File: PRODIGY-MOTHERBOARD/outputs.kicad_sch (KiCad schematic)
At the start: 20 parts, among them J10 GPIO, J11 SPI_OUT, J12 I2C, J13 CAN, J14 SERIAL, J15 12V OUT, J16 SERVO, J17 SERVO, J18 SERVO, J19 Ultrasonic, J20 MOTOR, J3 A_IN, J4 USB_A, J5 A_OUT, J6 Neopixel, J7 GPIO, J8 GPIO, J9 GPIO

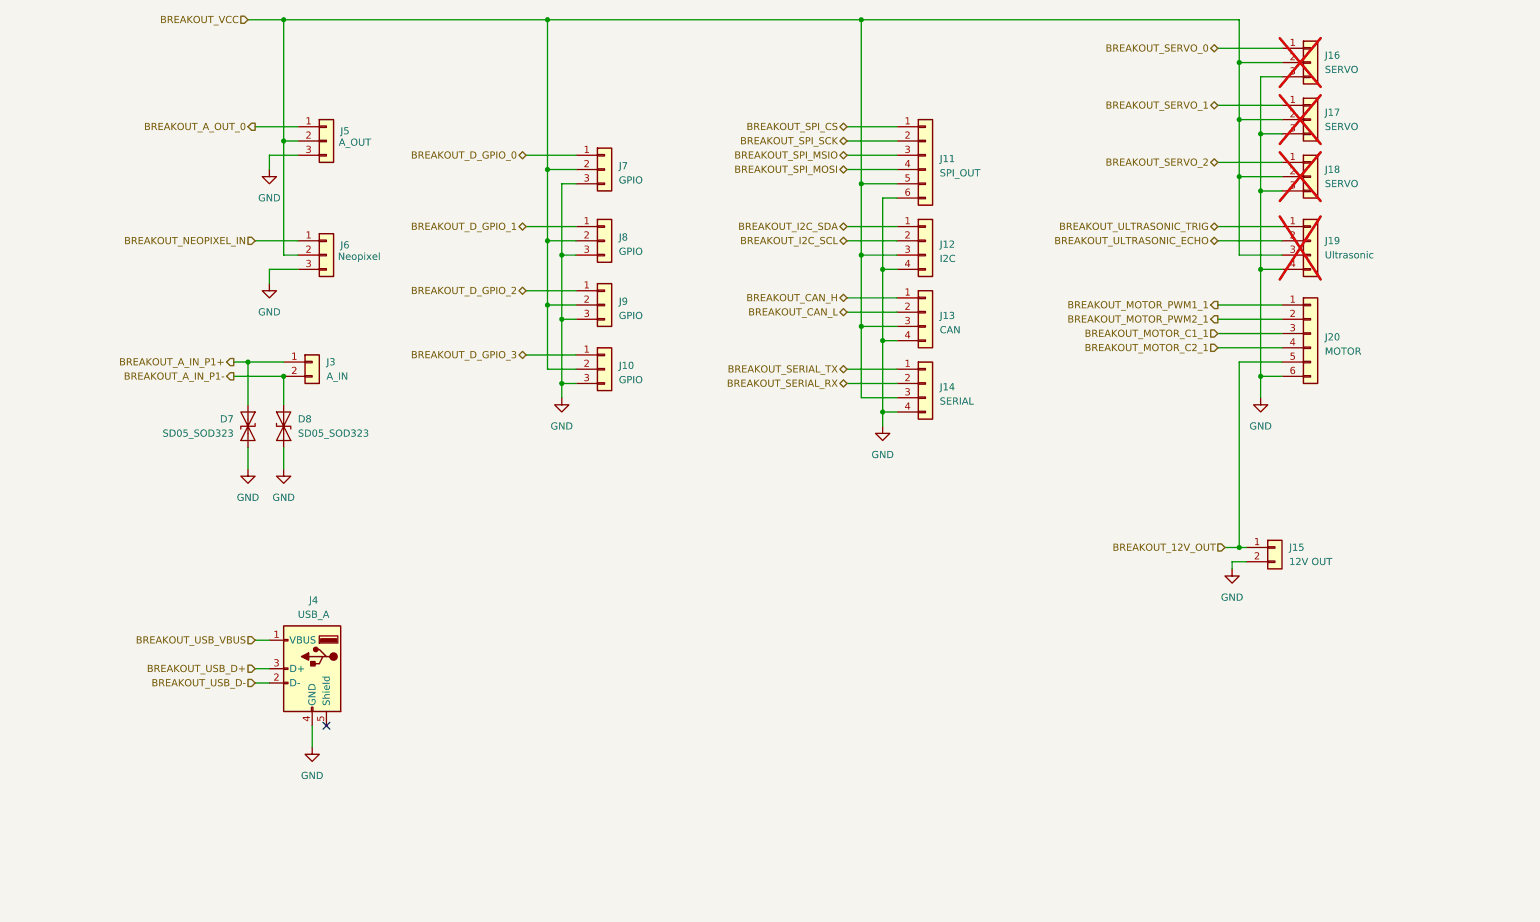
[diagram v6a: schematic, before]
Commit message: Added proper debounce filter elements to buttons.
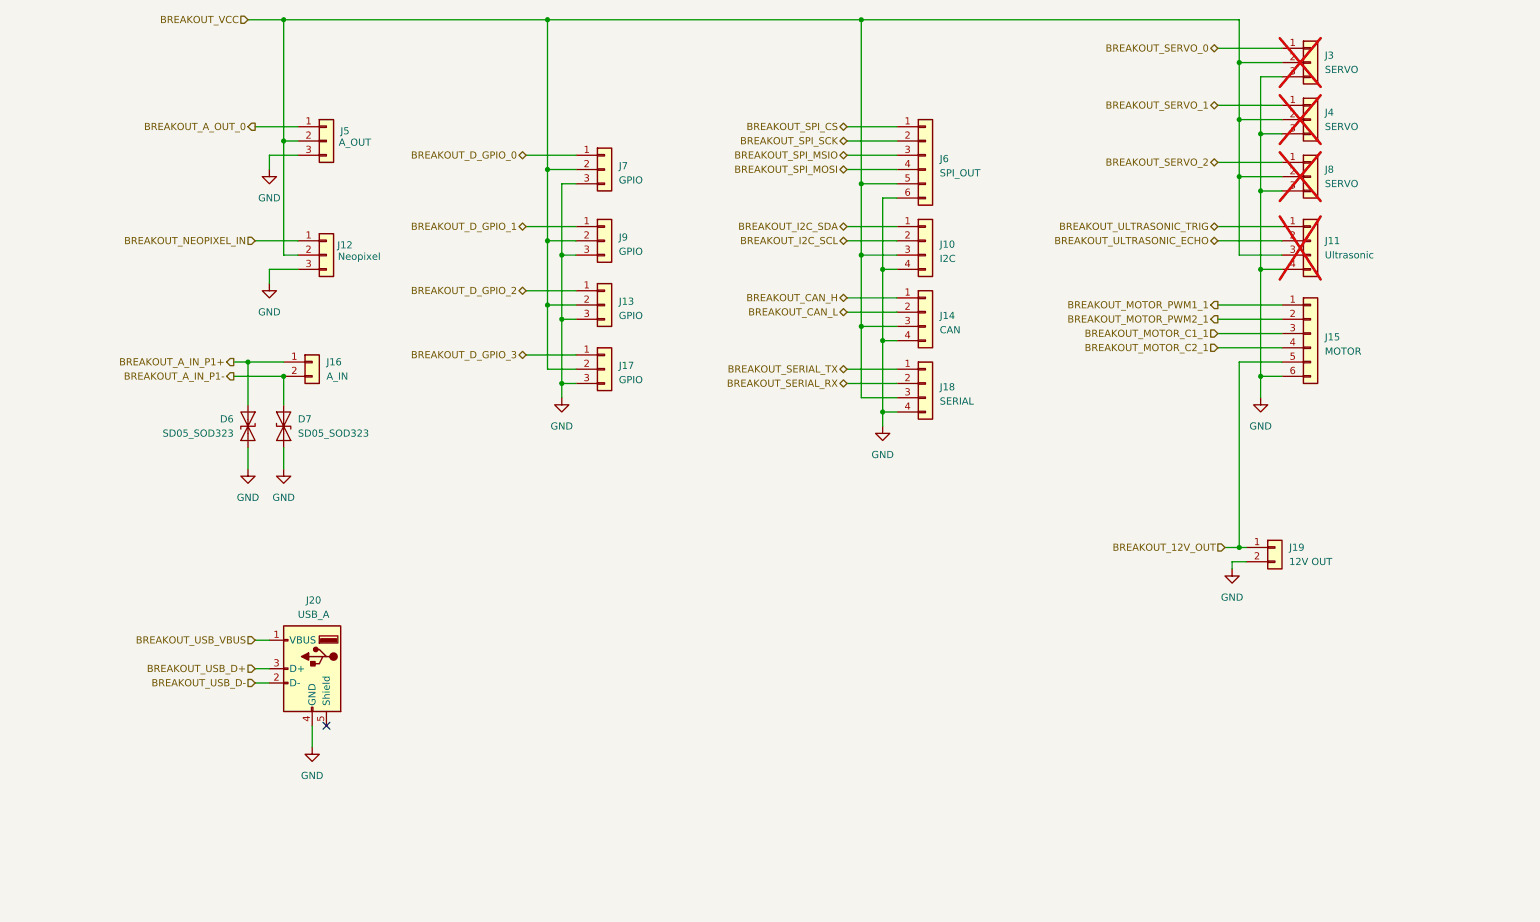
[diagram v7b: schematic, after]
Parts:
- renumbered D7 to D6, D8 to D7, J12 to J10, J19 to J11, J6 to J12, J9 to J13, J13 to J14, J20 to J15, J3 to J16, J10 to J17, J14 to J18, J15 to J19, J4 to J20, J16 to J3, J17 to J4, J11 to J6, J18 to J8, J8 to J9
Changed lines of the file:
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@@
 		(dnp no)
 		(fields_autoplaced yes)
-		(property "Reference" "#PWR013"
+		(property "Reference" "#PWR014"
 			(at 62.23 81.28 0)
 			(effects
@@
 			(project "PRODIGY-MOTHERBOARD"
 				(path "/f1c25860-8989-4190-bd24-2491d23ca7d9/a962dcec-9dee-4e54-acaa-e8da87dab487"
-					(reference "#PWR013")
+					(reference "#PWR014")
 					(unit 1)
 				)
@@
 		(dnp no)
 		(fields_autoplaced yes)
-		(property "Reference" "J20"
+		(property "Reference" "J15"
 			(at 250.19 84.455 0)
 			(effects
@@
 			(project "PRODIGY-MOTHERBOARD"
 				(path "/f1c25860-8989-4190-bd24-2491d23ca7d9/a962dcec-9dee-4e54-acaa-e8da87dab487"
-					(reference "J20")
+					(reference "J15")
 					(unit 1)
 				)
@@
 		(on_board yes)
 		(dnp no)
-		(property "Reference" "J4"
+		(property "Reference" "J20"
 			(at 70.104 131.318 0)
 			(effects
@@
 			(project "PRODIGY-MOTHERBOARD"
 				(path "/f1c25860-8989-4190-bd24-2491d23ca7d9/a962dcec-9dee-4e54-acaa-e8da87dab487"
-					(reference "J4")
+					(reference "J20")
 					(unit 1)
 				)
@@
 		(dnp no)
 		(fields_autoplaced yes)
-		(property "Reference" "#PWR018"
+		(property "Reference" "#PWR016"
 			(at 238.76 101.6 0)
 			(effects
@@
 			(project "PRODIGY-MOTHERBOARD"
 				(path "/f1c25860-8989-4190-bd24-2491d23ca7d9/a962dcec-9dee-4e54-acaa-e8da87dab487"
-					(reference "#PWR018")
+					(reference "#PWR016")
 					(unit 1)
 				)
@@
 		(dnp no)
 		(fields_autoplaced yes)
-		(property "Reference" "D7"
+		(property "Reference" "D6"
 			(at 55.88 99.0599 90)
 			(effects
@@
 			(project "PRODIGY-MOTHERBOARD"
 				(path "/f1c25860-8989-4190-bd24-2491d23ca7d9/a962dcec-9dee-4e54-acaa-e8da87dab487"
-					(reference "D7")
+					(reference "D6")
 					(unit 1)
 				)
@@
 		(dnp no)
 		(fields_autoplaced yes)
-		(property "Reference" "D8"
+		(property "Reference" "D7"
 			(at 67.31 99.0599 90)
 			(effects
@@
 			(project "PRODIGY-MOTHERBOARD"
 				(path "/f1c25860-8989-4190-bd24-2491d23ca7d9/a962dcec-9dee-4e54-acaa-e8da87dab487"
-					(reference "D8")
+					(reference "D7")
 					(unit 1)
 				)
@@
 		(dnp no)
 		(fields_autoplaced yes)
-		(property "Reference" "J9"
+		(property "Reference" "J13"
 			(at 124.46 78.105 0)
 			(effects
@@
 			(project "PRODIGY-MOTHERBOARD"
 				(path "/f1c25860-8989-4190-bd24-2491d23ca7d9/a962dcec-9dee-4e54-acaa-e8da87dab487"
-					(reference "J9")
+					(reference "J13")
 					(unit 1)
 				)
@@
 		(dnp no)
 		(fields_autoplaced yes)
-		(property "Reference" "J12"
+		(property "Reference" "J10"
 			(at 181.61 67.945 0)
 			(effects
@@
 			(project "PRODIGY-MOTHERBOARD"
 				(path "/f1c25860-8989-4190-bd24-2491d23ca7d9/a962dcec-9dee-4e54-acaa-e8da87dab487"
-					(reference "J12")
+					(reference "J10")
 					(unit 1)
 				)
@@
 		(dnp no)
 		(fields_autoplaced yes)
-		(property "Reference" "#PWR014"
+		(property "Reference" "#PWR021"
 			(at 69.85 163.83 0)
 			(effects
@@
 			(project "PRODIGY-MOTHERBOARD"
 				(path "/f1c25860-8989-4190-bd24-2491d23ca7d9/a962dcec-9dee-4e54-acaa-e8da87dab487"
-					(reference "#PWR014")
+					(reference "#PWR021")
 					(unit 1)
 				)
@@
 		(dnp yes)
 		(fields_autoplaced yes)
-		(property "Reference" "J16"
+		(property "Reference" "J3"
 			(at 250.19 34.2899 0)
 			(effects
@@
 			(project "PRODIGY-MOTHERBOARD"
 				(path "/f1c25860-8989-4190-bd24-2491d23ca7d9/a962dcec-9dee-4e54-acaa-e8da87dab487"
-					(reference "J16")
+					(reference "J3")
 					(unit 1)
 				)
@@
 		(dnp no)
 		(fields_autoplaced yes)
-		(property "Reference" "J15"
+		(property "Reference" "J19"
 			(at 243.84 121.9199 0)
 			(effects
@@
 			(project "PRODIGY-MOTHERBOARD"
 				(path "/f1c25860-8989-4190-bd24-2491d23ca7d9/a962dcec-9dee-4e54-acaa-e8da87dab487"
-					(reference "J15")
+					(reference "J19")
 					(unit 1)
 				)
@@
 		(dnp no)
 		(fields_autoplaced yes)
-		(property "Reference" "#PWR0114"
+		(property "Reference" "#PWR019"
 			(at 64.77 114.3 0)
 			(effects
@@
 			(project "PRODIGY-MOTHERBOARD"
 				(path "/f1c25860-8989-4190-bd24-2491d23ca7d9/a962dcec-9dee-4e54-acaa-e8da87dab487"
-					(reference "#PWR0114")
+					(reference "#PWR019")
 					(unit 1)
 				)
@@
 		(dnp no)
 		(fields_autoplaced yes)
-		(property "Reference" "#PWR016"
+		(property "Reference" "#PWR017"
 			(at 171.45 106.68 0)
 			(effects
@@
 			(project "PRODIGY-MOTHERBOARD"
 				(path "/f1c25860-8989-4190-bd24-2491d23ca7d9/a962dcec-9dee-4e54-acaa-e8da87dab487"
-					(reference "#PWR016")
+					(reference "#PWR017")
 					(unit 1)
 				)
@@
 		(dnp no)
 		(fields_autoplaced yes)
-		(property "Reference" "#PWR017"
+		(property "Reference" "#PWR020"
 			(at 233.68 132.08 0)
 			(effects
@@
 			(project "PRODIGY-MOTHERBOARD"
 				(path "/f1c25860-8989-4190-bd24-2491d23ca7d9/a962dcec-9dee-4e54-acaa-e8da87dab487"
-					(reference "#PWR017")
+					(reference "#PWR020")
 					(unit 1)
 				)
@@
 		(dnp yes)
 		(fields_autoplaced yes)
-		(property "Reference" "J17"
+		(property "Reference" "J4"
 			(at 250.19 44.4499 0)
 			(effects
@@
 			(project "PRODIGY-MOTHERBOARD"
 				(path "/f1c25860-8989-4190-bd24-2491d23ca7d9/a962dcec-9dee-4e54-acaa-e8da87dab487"
-					(reference "J17")
+					(reference "J4")
 					(unit 1)
 				)
@@
 		(dnp no)
 		(fields_autoplaced yes)
-		(property "Reference" "J3"
+		(property "Reference" "J16"
 			(at 72.39 88.8999 0)
 			(effects
@@
 			(project "PRODIGY-MOTHERBOARD"
 				(path "/f1c25860-8989-4190-bd24-2491d23ca7d9/a962dcec-9dee-4e54-acaa-e8da87dab487"
-					(reference "J3")
+					(reference "J16")
 					(unit 1)
 				)
@@
 		(dnp no)
 		(fields_autoplaced yes)
-		(property "Reference" "J8"
+		(property "Reference" "J9"
 			(at 124.46 66.675 0)
 			(effects
@@
 			(project "PRODIGY-MOTHERBOARD"
 				(path "/f1c25860-8989-4190-bd24-2491d23ca7d9/a962dcec-9dee-4e54-acaa-e8da87dab487"
-					(reference "J8")
+					(reference "J9")
 					(unit 1)
 				)
@@
 		(dnp yes)
 		(fields_autoplaced yes)
-		(property "Reference" "J18"
+		(property "Reference" "J8"
 			(at 250.19 54.6099 0)
 			(effects
@@
 			(project "PRODIGY-MOTHERBOARD"
 				(path "/f1c25860-8989-4190-bd24-2491d23ca7d9/a962dcec-9dee-4e54-acaa-e8da87dab487"
-					(reference "J18")
+					(reference "J8")
 					(unit 1)
 				)
@@
 		(dnp yes)
 		(fields_autoplaced yes)
-		(property "Reference" "J19"
+		(property "Reference" "J11"
 			(at 250.19 67.3099 0)
 			(effects
@@
 			(project "PRODIGY-MOTHERBOARD"
 				(path "/f1c25860-8989-4190-bd24-2491d23ca7d9/a962dcec-9dee-4e54-acaa-e8da87dab487"
-					(reference "J19")
+					(reference "J11")
 					(unit 1)
 				)
@@
 		(dnp no)
 		(fields_autoplaced yes)
-		(property "Reference" "J13"
+		(property "Reference" "J14"
 			(at 181.61 80.645 0)
 			(effects
@@
 			(project "PRODIGY-MOTHERBOARD"
 				(path "/f1c25860-8989-4190-bd24-2491d23ca7d9/a962dcec-9dee-4e54-acaa-e8da87dab487"
-					(reference "J13")
+					(reference "J14")
 					(unit 1)
 				)
@@
 		(dnp no)
 		(fields_autoplaced yes)
-		(property "Reference" "J11"
+		(property "Reference" "J6"
 			(at 181.61 52.705 0)
 			(effects
@@
 			(project "PRODIGY-MOTHERBOARD"
 				(path "/f1c25860-8989-4190-bd24-2491d23ca7d9/a962dcec-9dee-4e54-acaa-e8da87dab487"
-					(reference "J11")
+					(reference "J6")
 					(unit 1)
 				)
@@
 		(dnp no)
 		(fields_autoplaced yes)
-		(property "Reference" "#PWR058"
+		(property "Reference" "#PWR018"
 			(at 58.42 114.3 0)
 			(effects
@@
 			(project "PRODIGY-MOTHERBOARD"
 				(path "/f1c25860-8989-4190-bd24-2491d23ca7d9/a962dcec-9dee-4e54-acaa-e8da87dab487"
-					(reference "#PWR058")
+					(reference "#PWR018")
 					(unit 1)
 				)
@@
 		(on_board yes)
 		(dnp no)
-		(property "Reference" "J6"
+		(property "Reference" "J12"
 			(at 75.692 68.072 0)
 			(effects
@@
 			(project "PRODIGY-MOTHERBOARD"
 				(path "/f1c25860-8989-4190-bd24-2491d23ca7d9/a962dcec-9dee-4e54-acaa-e8da87dab487"
-					(reference "J6")
+					(reference "J12")
 					(unit 1)
 				)
@@
 		(dnp no)
 		(fields_autoplaced yes)
-		(property "Reference" "J10"
+		(property "Reference" "J17"
 			(at 124.46 89.535 0)
 			(effects
@@
 			(project "PRODIGY-MOTHERBOARD"
 				(path "/f1c25860-8989-4190-bd24-2491d23ca7d9/a962dcec-9dee-4e54-acaa-e8da87dab487"
-					(reference "J10")
+					(reference "J17")
 					(unit 1)
 				)
@@
 		(dnp no)
 		(fields_autoplaced yes)
-		(property "Reference" "J14"
+		(property "Reference" "J18"
 			(at 181.61 93.345 0)
 			(effects
@@
 			(project "PRODIGY-MOTHERBOARD"
 				(path "/f1c25860-8989-4190-bd24-2491d23ca7d9/a962dcec-9dee-4e54-acaa-e8da87dab487"
-					(reference "J14")
+					(reference "J18")
 					(unit 1)
 				)
@@
 		(dnp no)
 		(fields_autoplaced yes)
-		(property "Reference" "#PWR012"
+		(property "Reference" "#PWR013"
 			(at 62.23 60.96 0)
 			(effects
@@
 			(project "PRODIGY-MOTHERBOARD"
 				(path "/f1c25860-8989-4190-bd24-2491d23ca7d9/a962dcec-9dee-4e54-acaa-e8da87dab487"
-					(reference "#PWR012")
-					(unit 1)
-				)
+					(reference "#PWR013")
+					(unit 1)
+				)

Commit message: Submitted V0 for evaluation. Avaiting feedback.
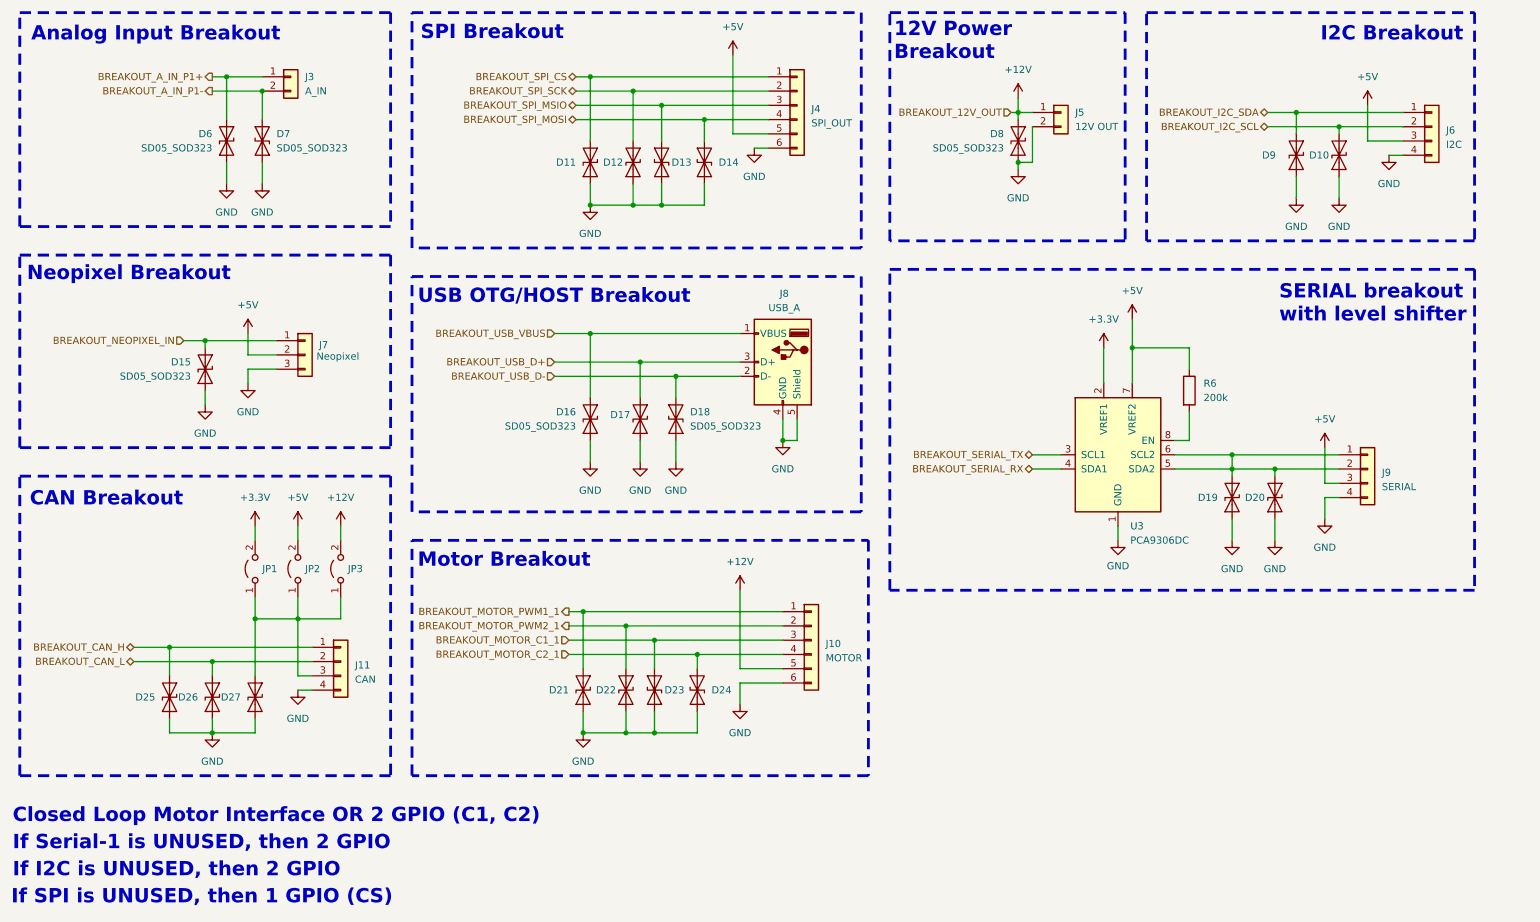
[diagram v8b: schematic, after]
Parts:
- removed J11: Ultrasonic, Connector_JST:JST_XH_S4B-XH-A_1x04_P2.50mm_Horizontal, symbol Connector_Generic:Conn_01x04
- removed J13, J17, J7, J9: GPIO, Connector_JST:JST_XH_S3B-XH-A_1x03_P2.50mm_Horizontal, symbol Connector_Generic:Conn_01x03
- removed J3, J4, J8: SERVO, Connector_JST:JST_XH_S3B-XH-A_1x03_P2.50mm_Horizontal, symbol Connector_Generic:Conn_01x03
- removed J5: A_OUT, Connector_JST:JST_XH_S3B-XH-A_1x03_P2.50mm_Horizontal, symbol Connector_Generic:Conn_01x03
- added D10, D11, D12, D13, D14, D15, D16, D17, D18, D19, D20, D21, D22, D23, D24, D25, D26, D27, D8, D9: SD05_SOD323, Diode_SMD:D_SOD-323, symbol Diode:SD05_SOD323
- added JP1, JP2, JP3: Jumper_2_Open, symbol Jumper:Jumper_2_Open
- added R6: 200k, symbol Device:R
- added U3: PCA9306DC, Package_SO:VSSOP-8_2.3x2mm_P0.5mm, symbol Interface:PCA9306DC
- J5: renamed from J19; value 12V OUT -> 12V OUT
- renumbered J15 to J10, J14 to J11, J16 to J3, J6 to J4, J10 to J6, J12 to J7, J20 to J8, J18 to J9
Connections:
- net BREAKOUT_CAN_H: now also D25.2 (A2)
- net BREAKOUT_CAN_L: now also D26.2 (A2)
- net BREAKOUT_I2C_SCL: now also D10.2 (A2)
- net BREAKOUT_I2C_SDA: now also D9.2 (A2)
- net BREAKOUT_MOTOR_C1_1: now also D23.2 (A2)
- net BREAKOUT_MOTOR_C2_1: now also D24.2 (A2)
- net BREAKOUT_MOTOR_PWM1_1: now also D21.2 (A2)
- net BREAKOUT_MOTOR_PWM2_1: now also D22.2 (A2)
- net BREAKOUT_NEOPIXEL_IN: now also D15.2 (A2)
- net BREAKOUT_SERIAL_RX: now also U3.4 (SDA1); no longer J9.2 (Pin_2)
- net BREAKOUT_SERIAL_TX: now also U3.3 (SCL1); no longer J9.1 (Pin_1)
- net BREAKOUT_SPI_CS: now also D11.2 (A2)
- net BREAKOUT_SPI_MOSI: now also D14.2 (A2)
- net BREAKOUT_SPI_MSIO: now also D13.2 (A2)
- net BREAKOUT_SPI_SCK: now also D12.2 (A2)
- net BREAKOUT_USB_D+: now also D17.2 (A2)
- net BREAKOUT_USB_D-: now also D18.2 (A2)
- net BREAKOUT_USB_VBUS: now also D16.2 (A2)
- net GND: now also J8.5 (Shield), D10.1 (A1), D11.1 (A1), D12.1 (A1), D13.1 (A1), D14.1 (A1), D15.1 (A1), D16.1 (A1), D17.1 (A1), D18.1 (A1), D19.1 (A1), D20.1 (A1), D21.1 (A1), D22.1 (A1), D23.1 (A1), D24.1 (A1), D25.1 (A1), D26.1 (A1), D27.1 (A1), D8.1 (A1), D9.1 (A1), U3.1 (GND)
- net BREAKOUT_12V_OUT renamed +12V
- net +12V: now also D8.2 (A2), JP3.2 (B)
- net BREAKOUT_VCC renamed +5V
- net +5V: now also JP2.2 (B), R6.1, U3.7 (VREF2); no longer J11.3 (Pin_3)
- new net: D19.2 (A2), D20.2 (A2), J9.1 (Pin_1), J9.2 (Pin_2), U3.5 (SDA2), U3.6 (SCL2)
- new net: R6.2, U3.8 (EN)
- new net: D27.2 (A2), J11.3 (Pin_3), JP1.1 (A), JP2.1 (A), JP3.1 (A)
- new net +3.3V: JP1.2 (B), U3.2 (VREF1)
- no-connect marks 1 -> 0
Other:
- note added: "12V Power Breakout"
- note added: "Analog Input Breakout"
- note added: "CAN Breakout"
- note added: "Closed Loop Motor Interface OR 2 GPIO (C1, C2)"
- note added: "I2C Breakout"
- note added: "If I2C is UNUSED, then 2 GPIO"
- note added: "If SPI is UNUSED, then 1 GPIO (CS)"
- note added: "If Serial-1 is UNUSED, then 2 GPIO"
- note added: "Motor Breakout"
- note added: "Neopixel Breakout"
- note added: "SERIAL breakout with level shifter"
- note added: "SPI Breakout"
- note added: "USB OTG/HOST Breakout"
- moved on the sheet: D6, D7, J10, J11, J3, J4, J5, J6, J7, J8, J9
